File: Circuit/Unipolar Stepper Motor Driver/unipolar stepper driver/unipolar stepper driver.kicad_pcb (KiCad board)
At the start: 2 copper layers, 18 parts, among them Q1 S8050, Q2 S8050, Q3 S8050, Q4 S8050

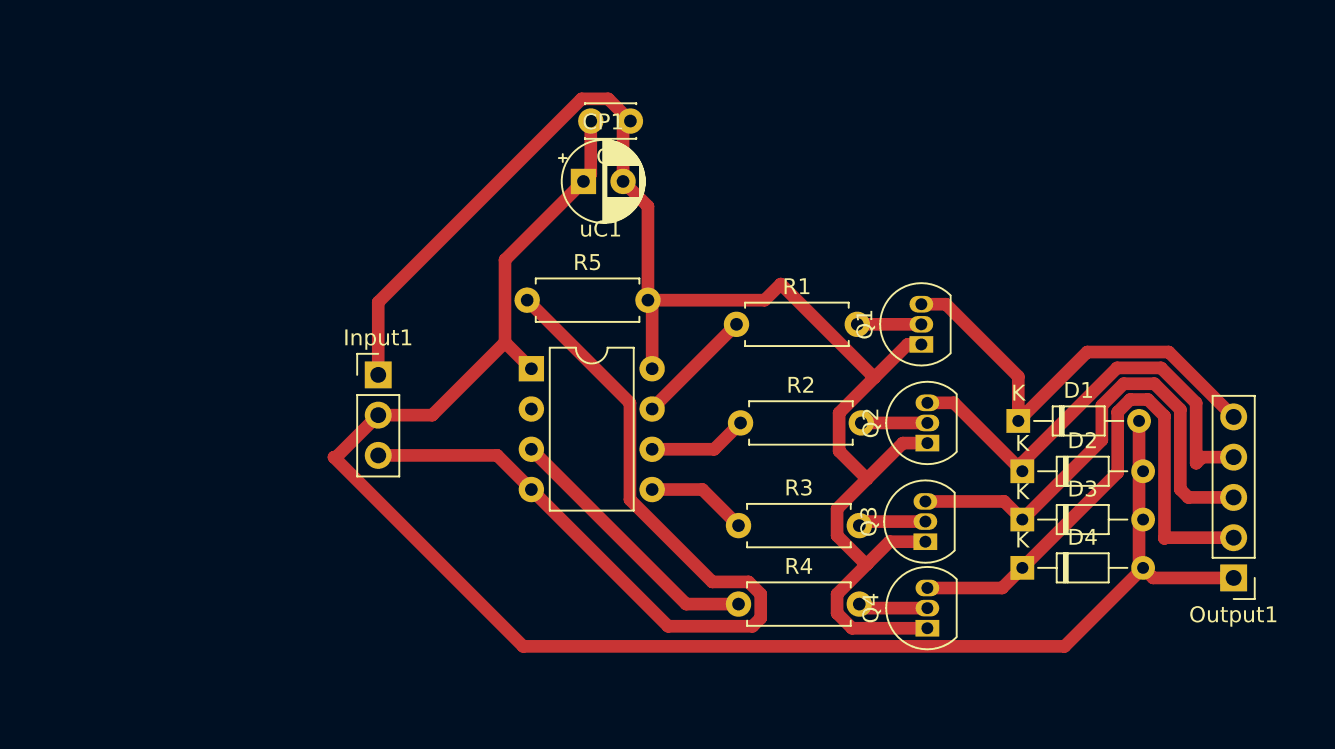
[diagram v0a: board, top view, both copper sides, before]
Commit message: Modified unipolar driver circuit and generated outputs
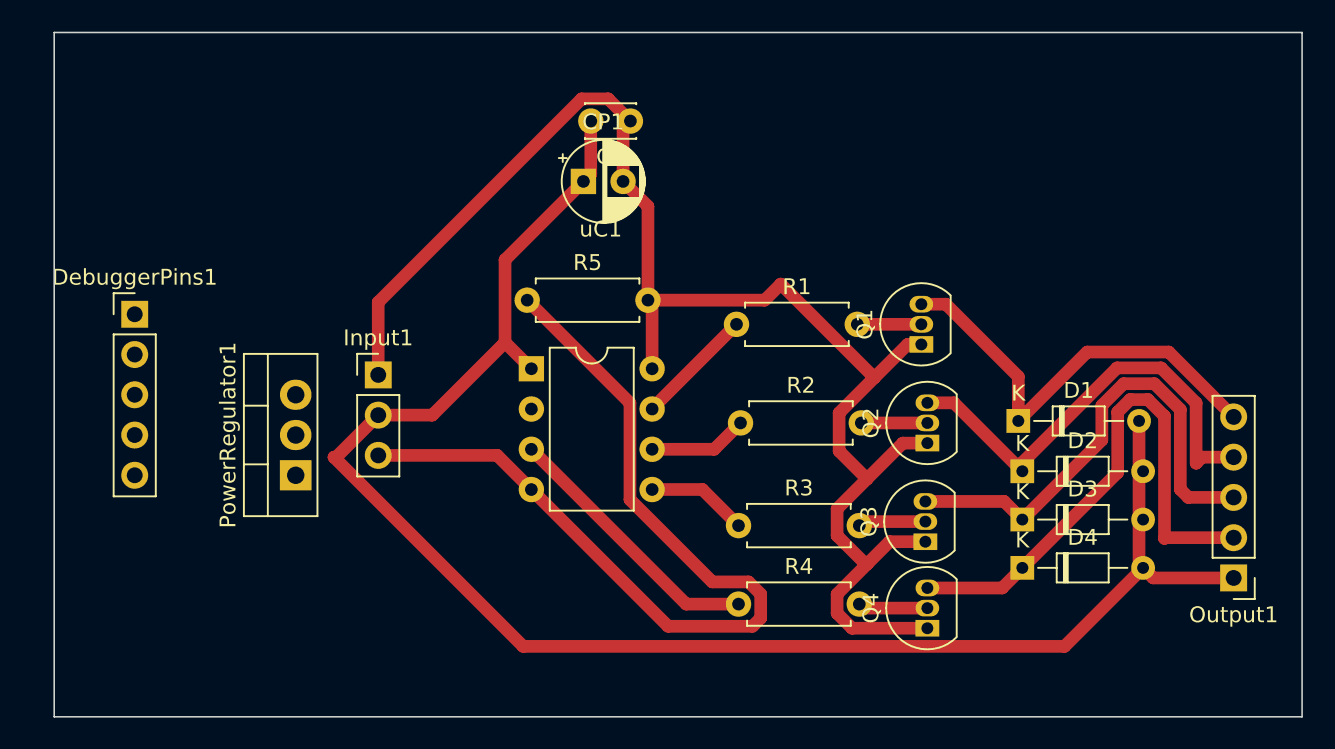
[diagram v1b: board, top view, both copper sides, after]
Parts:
- added DebuggerPins1: Conn_01x05_Female, Connector_PinHeader_2.54mm:PinHeader_1x05_P2.54mm_Vertical, F.Cu at (129.5, 94.0)
- added PowerRegulator1: LM7805_TO220, Package_TO_SOT_THT:TO-220-3_Vertical, F.Cu at (139.7, 104.1)
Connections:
- Input1 pad 2: +5V -> +12V
- R5 pad 1: Control_Input -> GND
- R5 pad 2: GND -> Control_Input
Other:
- board outline added: 78.7 x 43.2 mm
